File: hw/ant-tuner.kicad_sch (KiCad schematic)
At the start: 12 parts, among them K7703 G5Q-14-05, K7704 G5Q-14-05, K7705 G5Q-14-05, K7706 G5Q-14-05, U7713 TPIC6C595PWR

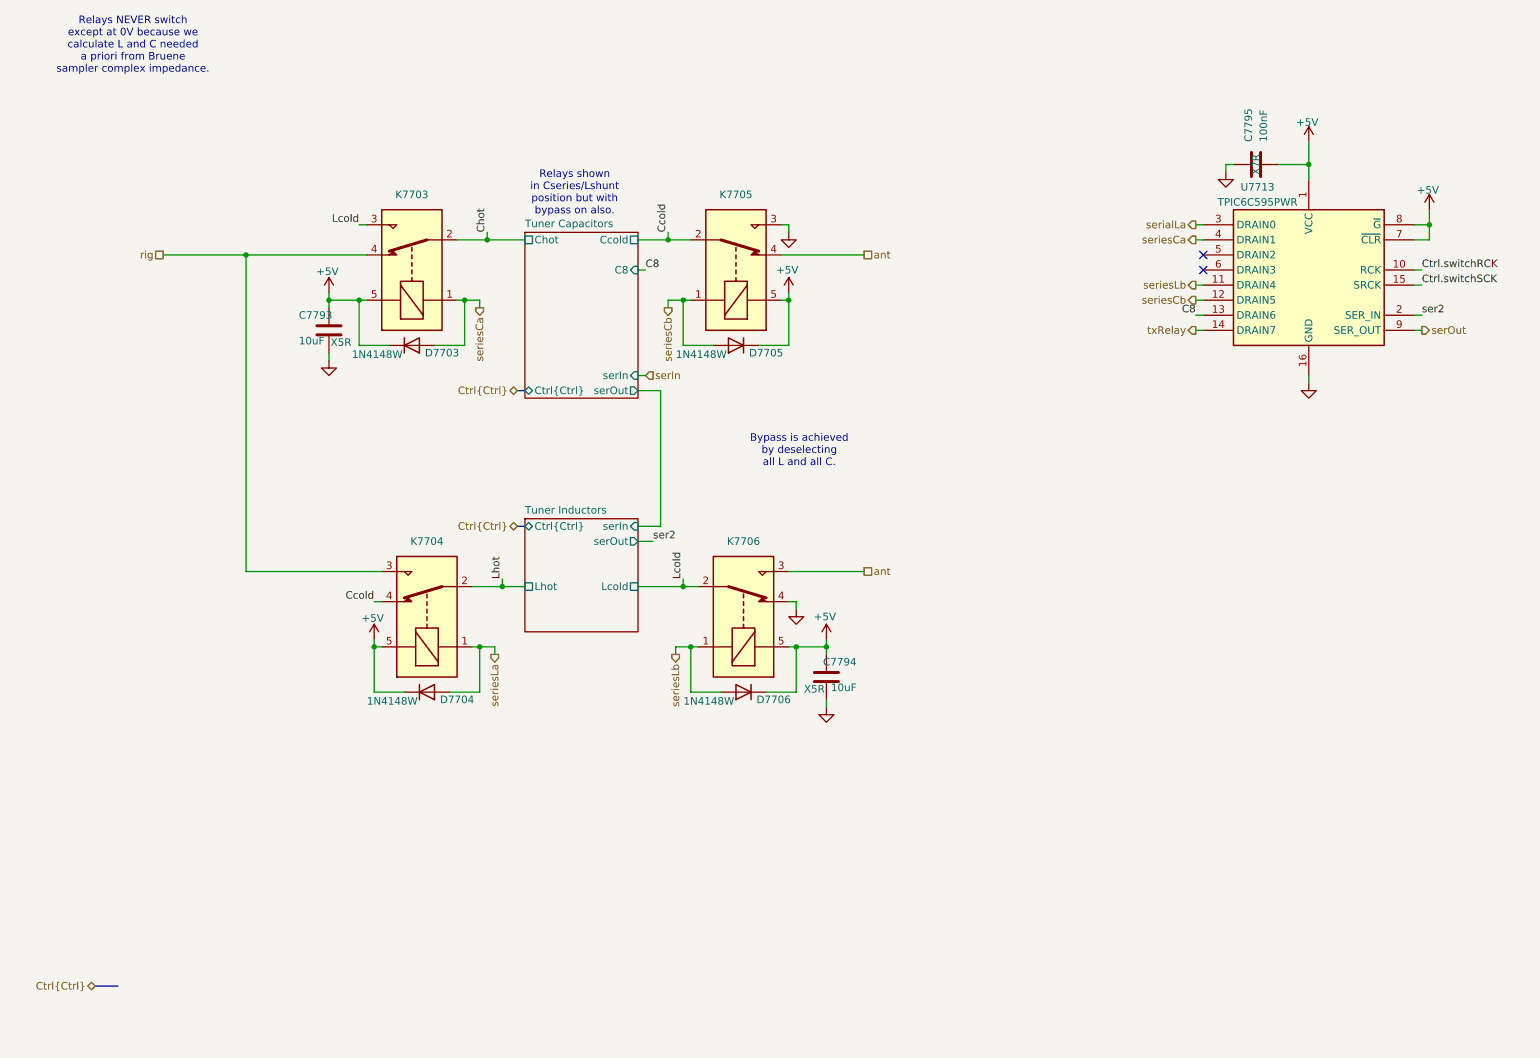
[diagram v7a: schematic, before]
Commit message: Clean up some footprints no longer used. Build footprints for LPF and antenna tuner inductors.
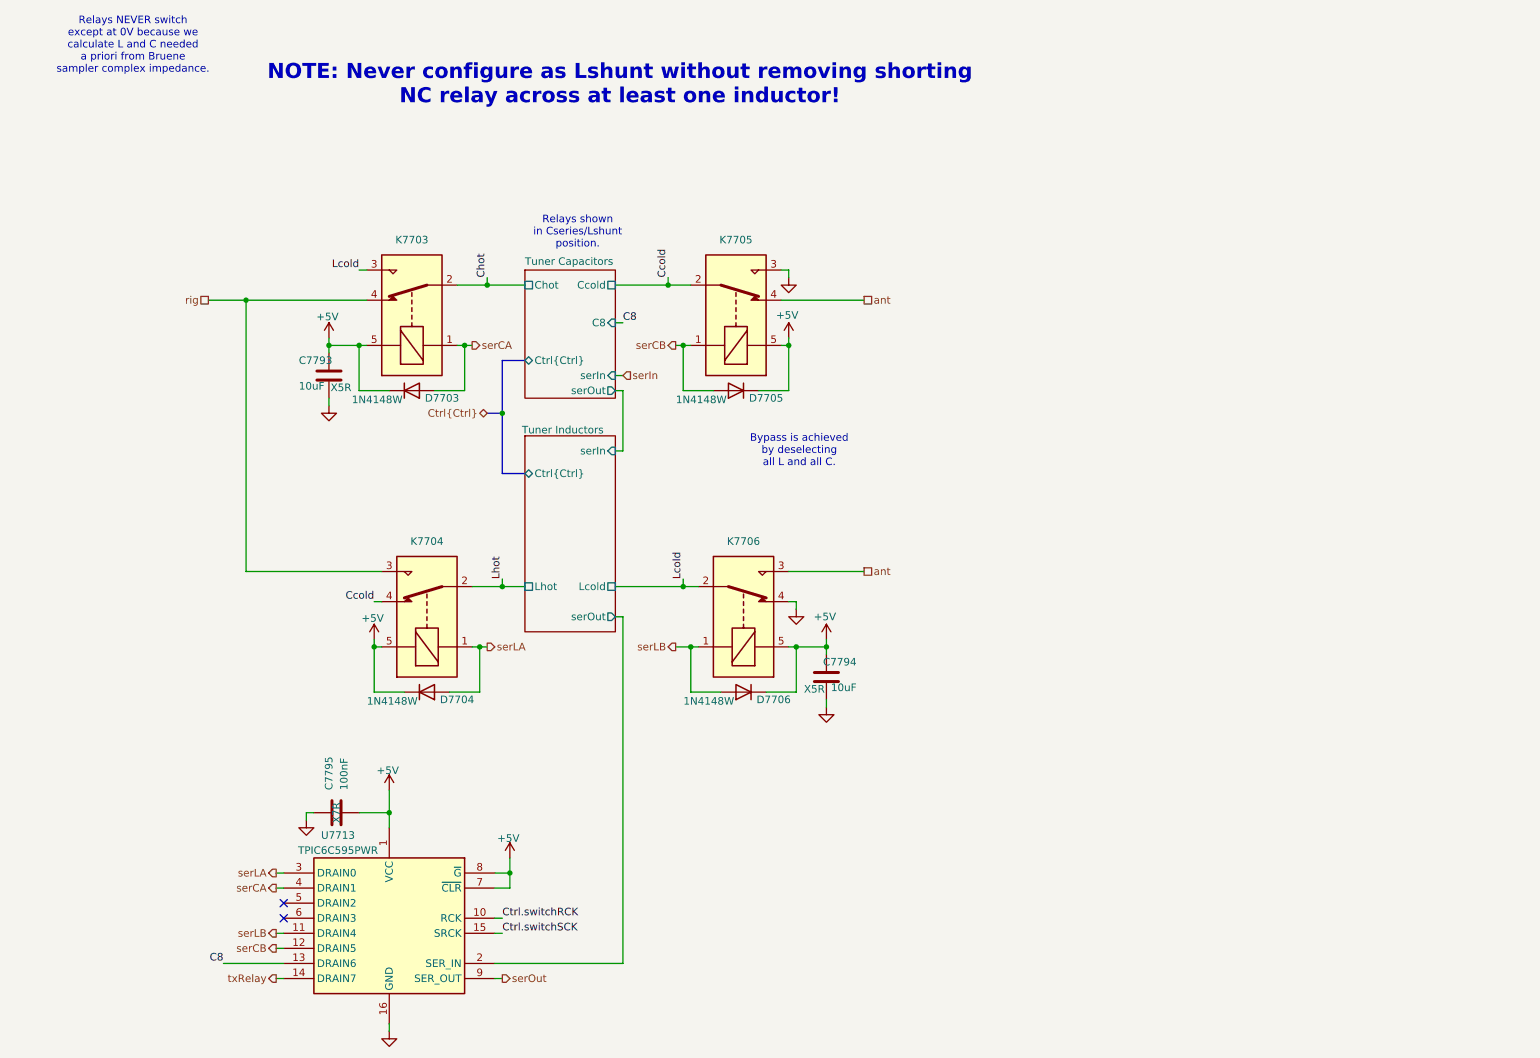
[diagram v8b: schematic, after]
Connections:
- net seriesLa is gone; now on net serLA: D7704.2 (A), K7704.1
- net ser2 renamed Tuner Inductors/serOut
- net serialLa renamed serLA
- net seriesCa renamed serCA
- net seriesCb renamed serCB
- net seriesLb renamed serLB
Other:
- note added: "NOTE: Never configure as Lshunt without removing shorting NC relay across at least one inductor!"
- note added: "Relays shown in Cseries/Lshunt position."
- note removed: "Relays shown in Cseries/Lshunt position but with bypass on also."
- moved on the sheet: C7793, C7795, D7703, D7705, K7703, K7705, U7713
